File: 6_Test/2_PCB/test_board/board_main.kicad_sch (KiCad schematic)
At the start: 4 parts, among them J1 PWR_Supply_Pins, J2 Analog_Input_Pins, J3 Digital_Input_Pins, J4 Digital_Output_Pins

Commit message: final draft of board, revision 2
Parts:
- removed J1: PWR_Supply_Pins, Connector_PinHeader_2.54mm:PinHeader_1x02_P2.54mm_Vertical, symbol Connector:Conn_01x02_Pin
- removed J2: Analog_Input_Pins, Connector_PinHeader_2.54mm:PinHeader_1x07_P2.54mm_Vertical, symbol Connector:Conn_01x07_Pin
- removed J3: Digital_Input_Pins, Connector_PinHeader_2.54mm:PinHeader_1x09_P2.54mm_Vertical, symbol Connector:Conn_01x09_Pin
- removed J4: Digital_Output_Pins, Connector_PinHeader_2.54mm:PinHeader_1x07_P2.54mm_Vertical, symbol Connector:Conn_01x07_Pin
- added J1: PWR_Supply_Pins, CONN_M20-99902_HRW, symbol 1x2Header:M20-9990245
- added J2: Analog_Input_Pins, CONN_PH1-07-UA_ADM, symbol 1x7Header:PH1-07-UA
- added J3: Digital_Input_Pins, CONN9_PH1_620x79_ADM, symbol 1x9Header:PH1-09-UA
- added J4: Digital_Output_Pins, CONN_PH1-07-UA_ADM, symbol 1x7Header:PH1-07-UA
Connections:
- net ADC/AVSS: now also J2.1
- net ADC/IN1: now also J2.7
- net ADC/IN2: now also J2.6
- net ADC/IN3: now also J2.5
- net ADC/IN4: now also J2.4
- net ADC/IN5: now also J2.3
- net ADC/IN6: now also J2.2
- net AnalogSupply/VSUP: now also J1.2
- net Buffer/CLK_IN1: now also J3.9
- net Buffer/CLK_IN2: now also J3.8
- net Buffer/CLK_IN3: now also J3.7
- net Buffer/CLK_IN4: now also J3.6
- net Buffer/CLK_IN5: now also J3.5
- net Buffer/CLK_IN6: now also J3.4
- net Buffer/CLK_IND: now also J3.3
- net Buffer/DO1: now also J4.1
- net Buffer/DO2: now also J4.2
- net Buffer/DO3: now also J4.3
- net Buffer/DO4: now also J4.4
- net Buffer/DO5: now also J4.5
- net Buffer/DO6: now also J4.6
- net Buffer/RES_IND: now also J3.2
- net GND: now also J1.1, J3.1, J4.7
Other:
- sheet Buffer ports: added IOVDD; removed VCC
- sheet ResetPulse ports: added IOVDD; removed V_SUP

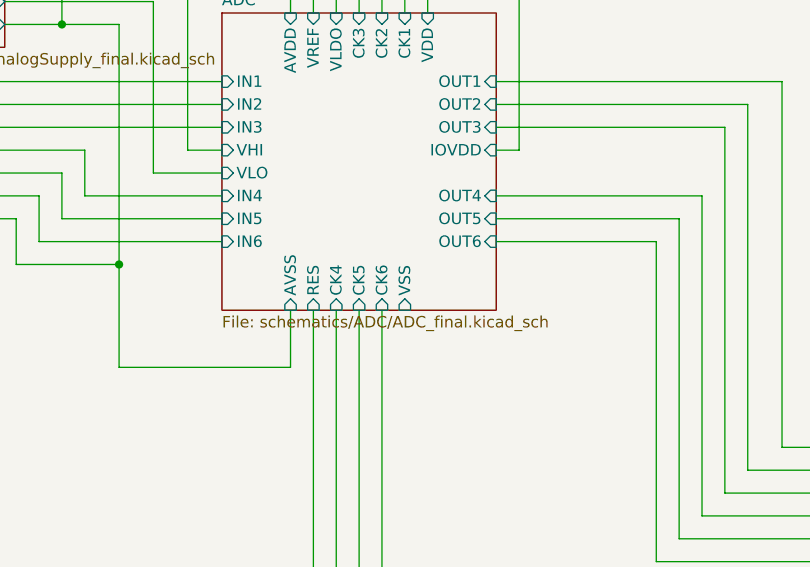
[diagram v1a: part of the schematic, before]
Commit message: DRC passing with all our components and pcbway rules
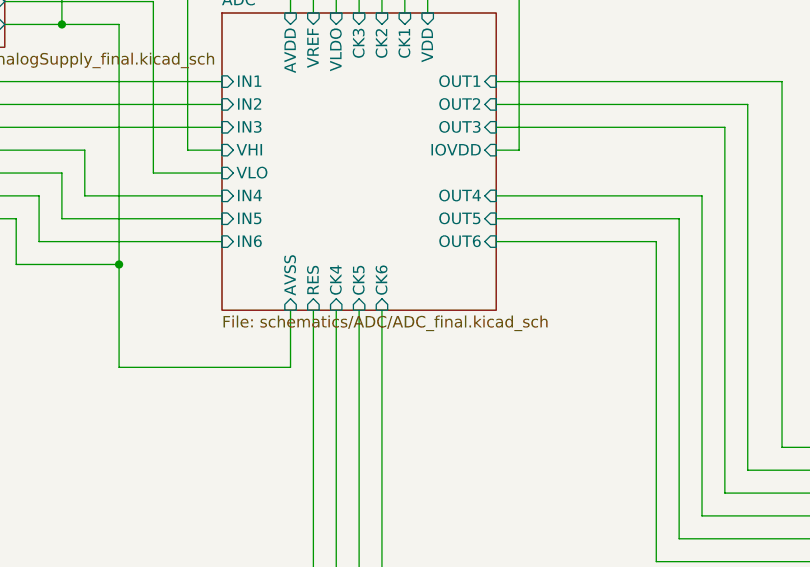
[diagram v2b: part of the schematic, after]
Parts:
- J1: footprint CONN_M20-99902_HRW -> ECE628_lib:1x2Header
- J2, J4: footprint CONN_PH1-07-UA_ADM -> ECE628_lib:1x7Header
- J3: footprint CONN9_PH1_620x79_ADM -> ECE628_lib:1x9Header
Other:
- sheet ADC ports: added none; removed VSS
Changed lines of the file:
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@@
 			)
 		)
-		(property "Footprint" "CONN_PH1-07-UA_ADM"
+		(property "Footprint" "ECE628_lib:1x7Header"
 			(at 336.55 147.32 0)
 			(effects
@@
 			)
 		)
-		(property "Footprint" "CONN_PH1-07-UA_ADM"
+		(property "Footprint" "ECE628_lib:1x7Header"
 			(at 119.38 121.92 0)
 			(effects
@@
 			)
 		)
-		(property "Footprint" "CONN9_PH1_620x79_ADM"
+		(property "Footprint" "ECE628_lib:1x9Header"
 			(at 120.65 200.66 0)
 			(effects
@@
 			)
 		)
-		(property "Footprint" "CONN_M20-99902_HRW"
+		(property "Footprint" "ECE628_lib:1x2Header"
 			(at 118.11 77.47 0)
 			(effects
@@
 			(effects
 				(font
-					(size 1.27 1.27)
-				)
-				(justify left)
-			)
-		)
-		(pin "VSS" input
-			(at 214.63 132.08 270)
-			(effects
-				(font

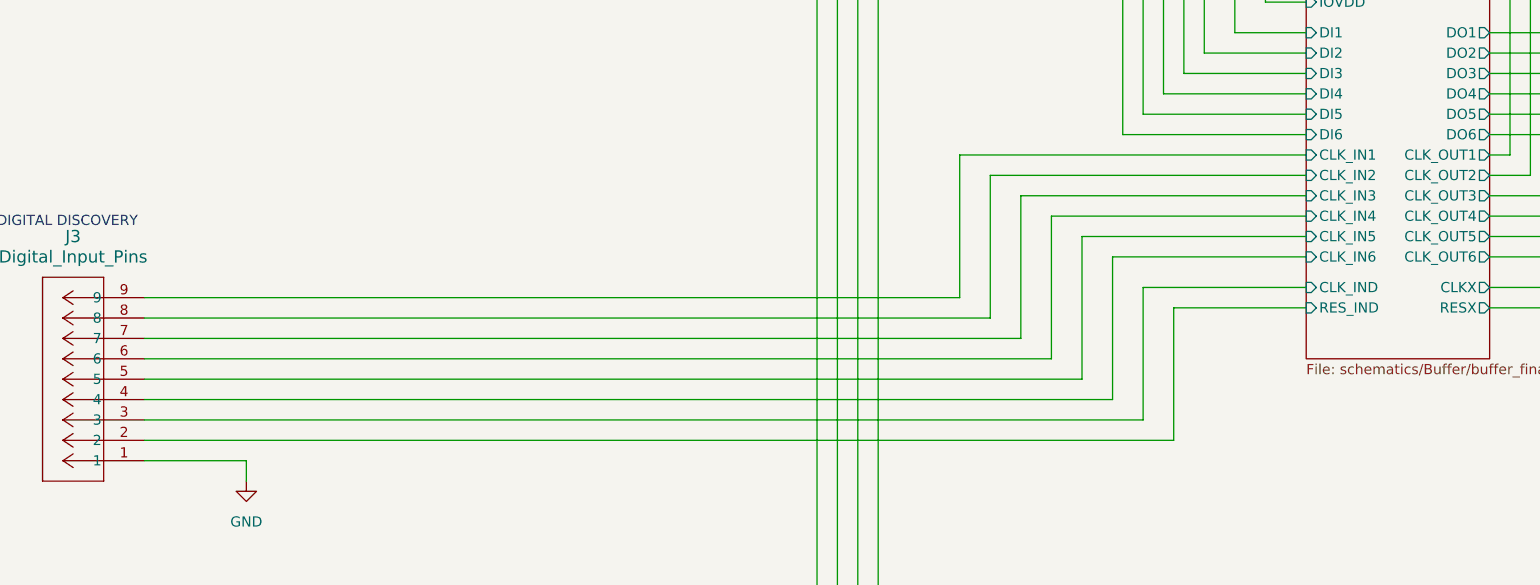
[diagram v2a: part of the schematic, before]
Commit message: Edit Layout 1_27
Rearranged the components in the layout and added majority of traces and ground layer. AVSS connections still need to be connected along with IOVDD
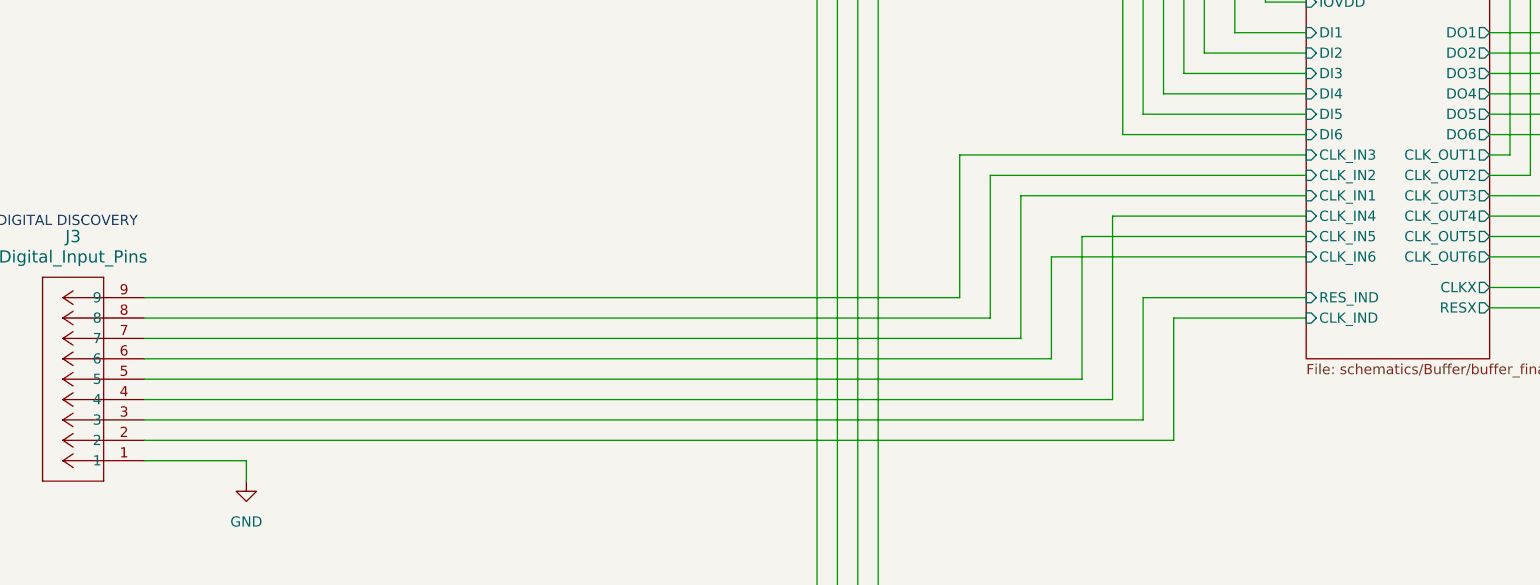
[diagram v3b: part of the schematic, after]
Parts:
- J1: footprint ECE628_lib:1x2Header -> Connector_PinHeader_2.54mm:PinHeader_1x02_P2.54mm_Vertical
- J2, J4: footprint ECE628_lib:1x7Header -> Connector_PinHeader_2.54mm:PinHeader_1x07_P2.54mm_Vertical
- J3: footprint ECE628_lib:1x9Header -> Connector_PinHeader_2.54mm:PinHeader_1x09_P2.54mm_Vertical
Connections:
- net Buffer/CLK_IN1: now also J3.7; no longer J3.9
- net Buffer/CLK_IN3: now also J3.9; no longer J3.7
- net Buffer/CLK_IN4: now also J3.4; no longer J3.6
- net Buffer/CLK_IN6: now also J3.6; no longer J3.4
- net Buffer/CLK_IND: now also J3.2; no longer J3.3
- net Buffer/RES_IND: now also J3.3; no longer J3.2

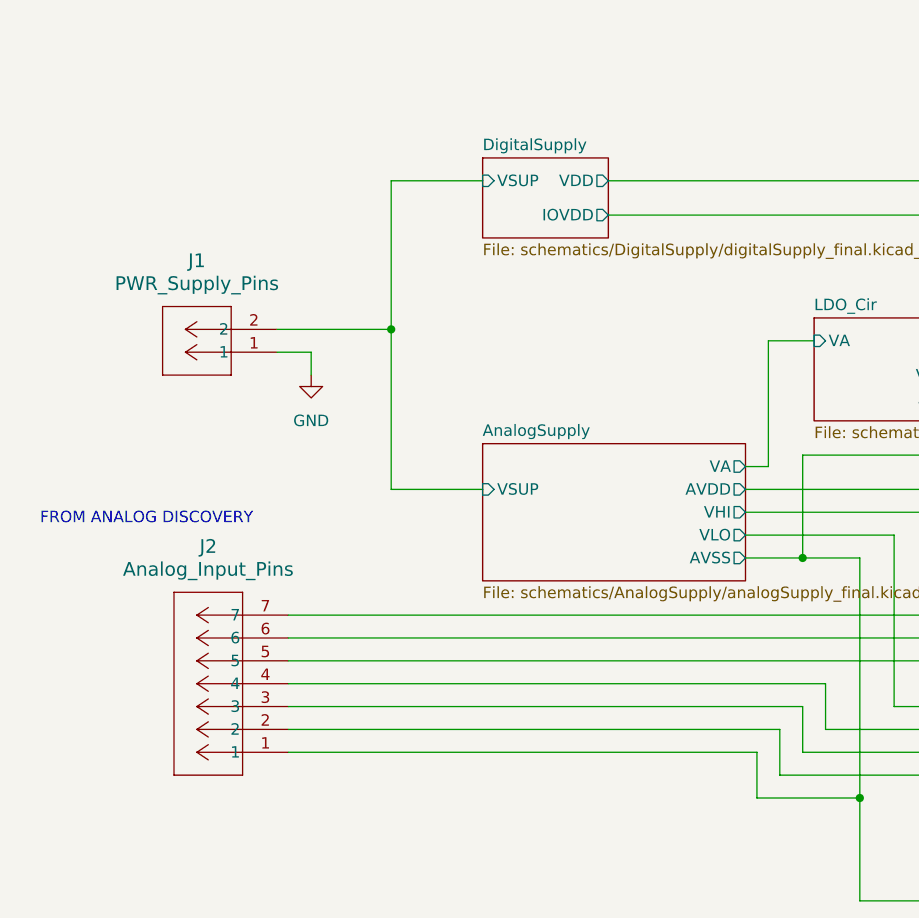
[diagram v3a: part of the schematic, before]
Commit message: Board Edits 250206
- Added the terminal block (4 positions - VSUP, GND, GND, & AVSS)
- Added vias for test points
- Added silkscreen labels for all inputs, jumpers, and potentiometers
- Widened traces going across the board
- Relabeled plane as AVSS plane
- Fixes to 3D model of board
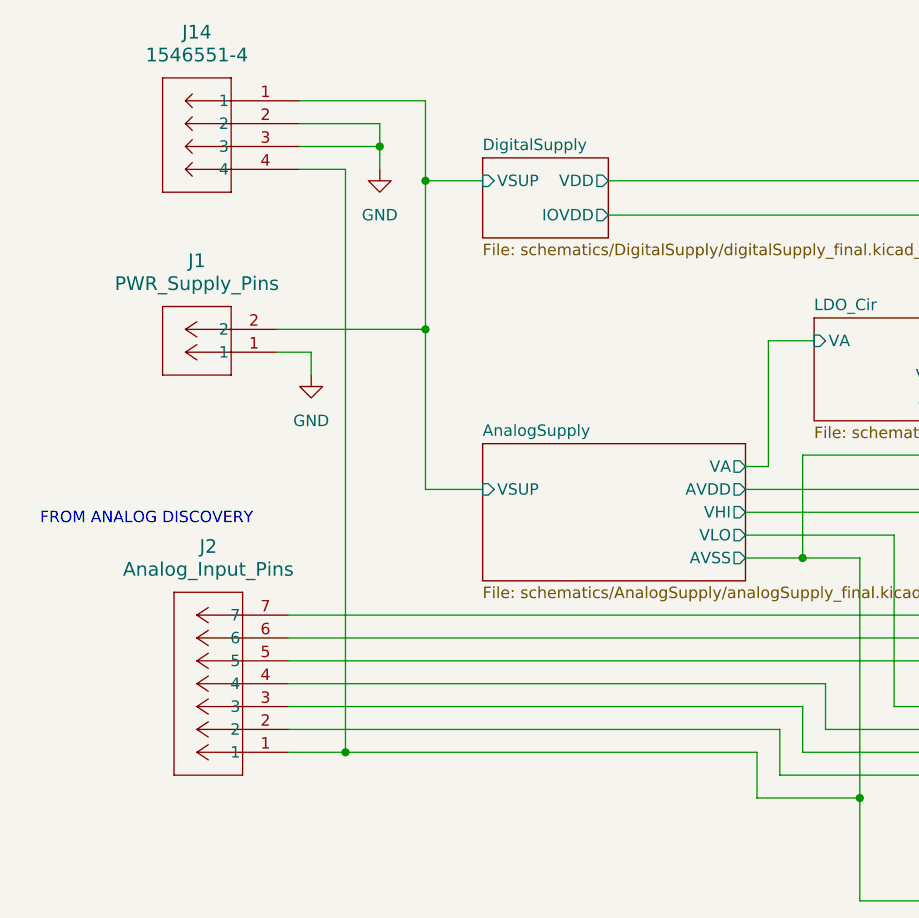
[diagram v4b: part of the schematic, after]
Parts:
- added J14: 1546551-4, TermBlck_4posFootprints:CONN4_1546551-4_TEC, symbol TermBlck_4pos:1546551-4
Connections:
- net ADC/AVSS: now also J14.4
- net AnalogSupply/VSUP: now also J14.1
- net GND: now also J14.2, J14.3
